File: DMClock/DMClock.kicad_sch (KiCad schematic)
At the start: 0 parts

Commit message: adding mplabxide init files
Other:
- sheet Power ports: added HV; removed none
- sheet User Interface ports: added none; removed 9V, Barrel Jack, Battery
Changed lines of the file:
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@@
 (kicad_sch (version 20230121) (generator eeschema)
   (paper "A4")
-  (sheet (at 59.69 99.568) (size 21.844 14.478) (fields_autoplaced)
+  (wire (pts (xy 96.266 49.53) (xy 116.586 49.53))
+    (stroke (width 0) (type default))
+  )
+  (wire (pts (xy 116.586 49.53) (xy 116.586 49.276))
+    (stroke (width 0) (type default))
+  )
+  (sheet (at 72.898 74.803) (size 21.844 14.478) (fields_autoplaced)
     (stroke (width 0.1524) (type solid))
     (fill (color 0 0 0 0.0000))
-    (property "Sheetname" "RTC" (at 59.69 98.8564 0)
+    (property "Sheetname" "RTC" (at 72.898 74.0914 0)
       (effects (font (size 1.27 1.27)) (justify left bottom))
     )
-    (property "Sheetfile" "rtc.kicad_sch" (at 59.69 114.6306 0)
+    (property "Sheetfile" "rtc.kicad_sch" (at 72.898 89.8656 0)
       (effects (font (size 1.27 1.27)) (justify left top))
     )
@@
     )
   )
-  (sheet (at 117.221 47.625) (size 28.067 15.367) (fields_autoplaced)
+  (sheet (at 116.586 48.133) (size 28.067 15.367) (fields_autoplaced)
     (stroke (width 0.1524) (type solid))
     (fill (color 0 0 0 0.0000))
-    (property "Sheetname" "User Interface" (at 117.221 46.9134 0)
+    (property "Sheetname" "User Interface" (at 116.586 47.4214 0)
       (effects (font (size 1.27 1.27)) (justify left bottom))
     )
-    (property "Sheetfile" "ui.kicad_sch" (at 117.221 63.5766 0)
+    (property "Sheetfile" "ui.kicad_sch" (at 116.586 64.0846 0)
       (effects (font (size 1.27 1.27)) (justify left top))
     )
-    (pin "HV" input (at 117.221 51.689 180)
-      (effects (font (size 1.27 1.27)) (justify left))
-    )
-    (pin "Battery" input (at 122.428 62.992 270)
-      (effects (font (size 1.27 1.27)) (justify left))
-    )
-    (pin "9V" input (at 117.221 53.34 180)
-      (effects (font (size 1.27 1.27)) (justify left))
-    )
-    (pin "Barrel Jack" input (at 124.206 62.992 270)
+    (pin "HV" input (at 116.586 49.276 180)
       (effects (font (size 1.27 1.27)) (justify left))
     )
@@
       (effects (font (size 1.27 1.27)) (justify left top))
     )
+    (pin "HV" output (at 96.266 49.53 0)
+      (effects (font (size 1.27 1.27)) (justify right))
+    )
     (instances

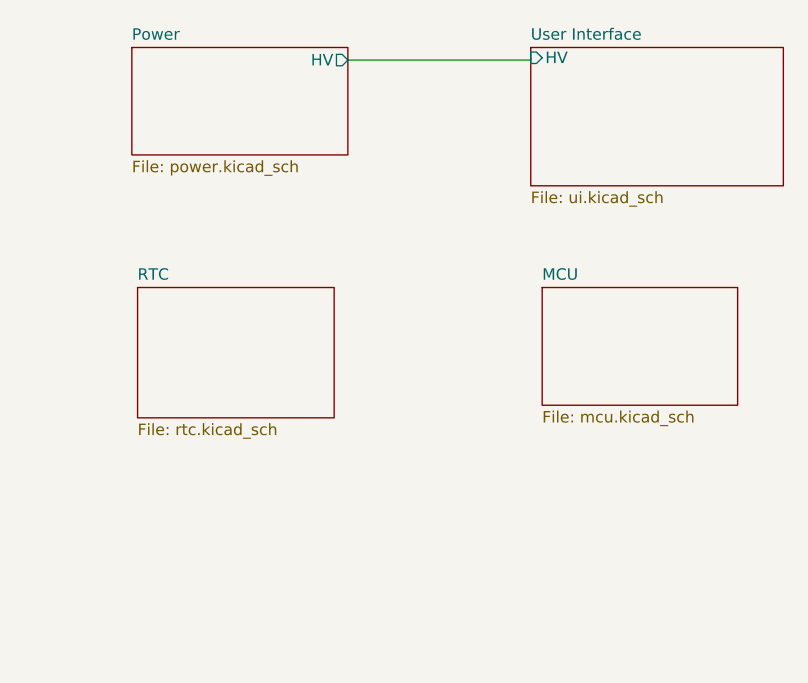
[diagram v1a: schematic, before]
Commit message: more modules added, still need to add a lot of footprints and see if there exist any sd card libraries for use with i2s
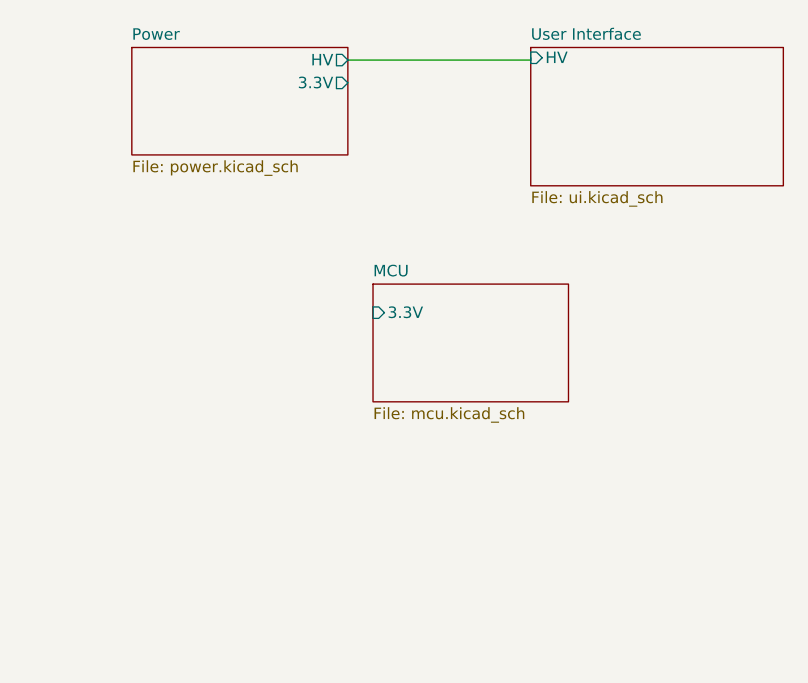
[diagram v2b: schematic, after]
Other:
- removed sheet RTC
- sheet MCU ports: added 3.3V; removed none
- sheet Power ports: added 3.3V; removed none
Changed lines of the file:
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@@
     (stroke (width 0) (type default))
-  )
-  (sheet (at 72.898 74.803) (size 21.844 14.478) (fields_autoplaced)
-    (stroke (width 0.1524) (type solid))
-    (fill (color 0 0 0 0.0000))
-    (property "Sheetname" "RTC" (at 72.898 74.0914 0)
-      (effects (font (size 1.27 1.27)) (justify left bottom))
-    )
-    (property "Sheetfile" "rtc.kicad_sch" (at 72.898 89.8656 0)
-      (effects (font (size 1.27 1.27)) (justify left top))
-    )
-    (instances
-      (project "DMClock"
-        (path "/b42b345f-a3f2-4eff-9109-2f4619119d33" (page "3"))
-      )
-    )
   )
   (sheet (at 116.586 48.133) (size 28.067 15.367) (fields_autoplaced)
@@
     )
   )
-  (sheet (at 117.856 74.803) (size 21.717 13.081) (fields_autoplaced)
+  (sheet (at 99.06 74.422) (size 21.717 13.081) (fields_autoplaced)
     (stroke (width 0.1524) (type solid))
     (fill (color 0 0 0 0.0000))
-    (property "Sheetname" "MCU" (at 117.856 74.0914 0)
+    (property "Sheetname" "MCU" (at 99.06 73.7104 0)
       (effects (font (size 1.27 1.27)) (justify left bottom))
     )
-    (property "Sheetfile" "mcu.kicad_sch" (at 117.856 88.4686 0)
+    (property "Sheetfile" "mcu.kicad_sch" (at 99.06 88.0876 0)
       (effects (font (size 1.27 1.27)) (justify left top))
+    )
+    (pin "3.3V" input (at 99.06 77.597 180)
+      (effects (font (size 1.27 1.27)) (justify left))
     )
     (instances
@@
       (effects (font (size 1.27 1.27)) (justify right))
     )
+    (pin "3.3V" output (at 96.266 52.07 0)
+      (effects (font (size 1.27 1.27)) (justify right))
+    )

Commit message: need to work on hvps logic converter
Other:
- sheet MCU ports: added CLK, HV5622DataIn, NOTBL, NOTLE; removed none
- sheet Power ports: added 12V; removed none
- sheet User Interface ports: added 12V, CLK, HV5622DataIn, NOTBL, NOTLE; removed none
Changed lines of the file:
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@@
 (kicad_sch (version 20230121) (generator eeschema)
   (paper "A4")
+  (wire (pts (xy 131.953 76.454) (xy 131.953 63.5))
+    (stroke (width 0) (type default))
+  )
+  (wire (pts (xy 97.79 52.07) (xy 97.79 77.597))
+    (stroke (width 0) (type default))
+  )
+  (wire (pts (xy 120.777 81.407) (xy 136.906 81.407))
+    (stroke (width 0) (type default))
+  )
+  (wire (pts (xy 120.777 76.454) (xy 131.953 76.454))
+    (stroke (width 0) (type default))
+  )
+  (wire (pts (xy 109.474 61.087) (xy 109.474 74.422))
+    (stroke (width 0) (type default))
+  )
+  (wire (pts (xy 97.79 77.597) (xy 99.06 77.597))
+    (stroke (width 0) (type default))
+  )
   (wire (pts (xy 96.266 49.53) (xy 116.586 49.53))
     (stroke (width 0) (type default))
   )
+  (wire (pts (xy 96.266 54.737) (xy 116.586 54.737))
+    (stroke (width 0) (type default))
+  )
+  (wire (pts (xy 96.266 52.07) (xy 97.79 52.07))
+    (stroke (width 0) (type default))
+  )
   (wire (pts (xy 116.586 49.53) (xy 116.586 49.276))
+    (stroke (width 0) (type default))
+  )
+  (wire (pts (xy 116.586 61.087) (xy 109.474 61.087))
+    (stroke (width 0) (type default))
+  )
+  (wire (pts (xy 134.366 78.867) (xy 120.777 78.867))
+    (stroke (width 0) (type default))
+  )
+  (wire (pts (xy 134.366 63.5) (xy 134.366 78.867))
+    (stroke (width 0) (type default))
+  )
+  (wire (pts (xy 136.906 81.407) (xy 136.906 63.5))
     (stroke (width 0) (type default))
   )
@@
     )
     (pin "HV" input (at 116.586 49.276 180)
+      (effects (font (size 1.27 1.27)) (justify left))
+    )
+    (pin "NOTBL" input (at 134.366 63.5 270)
+      (effects (font (size 1.27 1.27)) (justify left))
+    )
+    (pin "HV5622DataIn" input (at 136.906 63.5 270)
+      (effects (font (size 1.27 1.27)) (justify left))
+    )
+    (pin "NOTLE" input (at 131.953 63.5 270)
+      (effects (font (size 1.27 1.27)) (justify left))
+    )
+    (pin "CLK" input (at 116.586 61.087 180)
+      (effects (font (size 1.27 1.27)) (justify left))
+    )
+    (pin "12V" input (at 116.586 54.737 180)
       (effects (font (size 1.27 1.27)) (justify left))
     )
@@
     (pin "3.3V" input (at 99.06 77.597 180)
       (effects (font (size 1.27 1.27)) (justify left))
+    )
+    (pin "CLK" output (at 109.474 74.422 90)
+      (effects (font (size 1.27 1.27)) (justify right))
+    )
+    (pin "NOTLE" output (at 120.777 76.454 0)
+      (effects (font (size 1.27 1.27)) (justify right))
+    )
+    (pin "HV5622DataIn" output (at 120.777 81.407 0)
+      (effects (font (size 1.27 1.27)) (justify right))
+    )
+    (pin "NOTBL" output (at 120.777 78.867 0)
+      (effects (font (size 1.27 1.27)) (justify right))
     )
     (instances
@@
       (effects (font (size 1.27 1.27)) (justify right))
     )
+    (pin "12V" output (at 96.266 54.737 0)
+      (effects (font (size 1.27 1.27)) (justify right))
+    )

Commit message: just need to finish pcb
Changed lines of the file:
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@@
 (kicad_sch (version 20230121) (generator eeschema)
   (paper "A4")
-  (wire (pts (xy 131.953 76.454) (xy 131.953 63.5))
+  (wire (pts (xy 131.953 77.597) (xy 131.953 63.5))
     (stroke (width 0) (type default))
   )
@@
     (stroke (width 0) (type default))
   )
-  (wire (pts (xy 120.777 76.454) (xy 131.953 76.454))
+  (wire (pts (xy 120.777 77.597) (xy 131.953 77.597))
     (stroke (width 0) (type default))
   )
@@
     (stroke (width 0) (type default))
   )
-  (wire (pts (xy 134.366 78.867) (xy 120.777 78.867))
+  (wire (pts (xy 134.366 79.502) (xy 120.777 79.502))
     (stroke (width 0) (type default))
   )
-  (wire (pts (xy 134.366 63.5) (xy 134.366 78.867))
+  (wire (pts (xy 134.366 63.5) (xy 134.366 79.502))
     (stroke (width 0) (type default))
   )
@@
       (effects (font (size 1.27 1.27)) (justify right))
     )
-    (pin "NOTLE" output (at 120.777 76.454 0)
+    (pin "NOTLE" output (at 120.777 77.597 0)
       (effects (font (size 1.27 1.27)) (justify right))
     )
@@
       (effects (font (size 1.27 1.27)) (justify right))
     )
-    (pin "NOTBL" output (at 120.777 78.867 0)
+    (pin "NOTBL" output (at 120.777 79.502 0)
       (effects (font (size 1.27 1.27)) (justify right))
     )
